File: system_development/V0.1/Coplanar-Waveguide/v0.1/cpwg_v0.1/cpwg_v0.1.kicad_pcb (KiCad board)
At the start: 2 copper layers, 50 x 20 mm, 8 parts, among them J1 142-0761-801, J2 142-0761-801

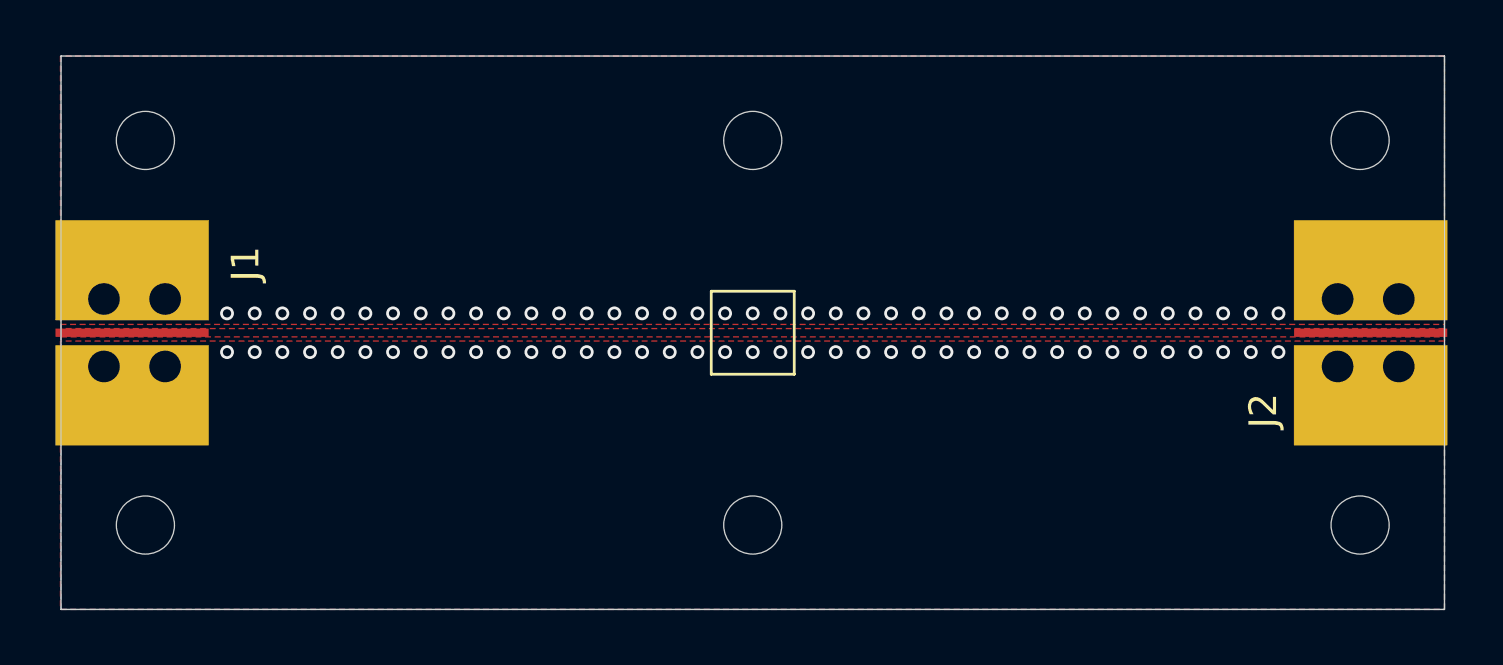
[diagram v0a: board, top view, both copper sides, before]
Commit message: updated silkscreen
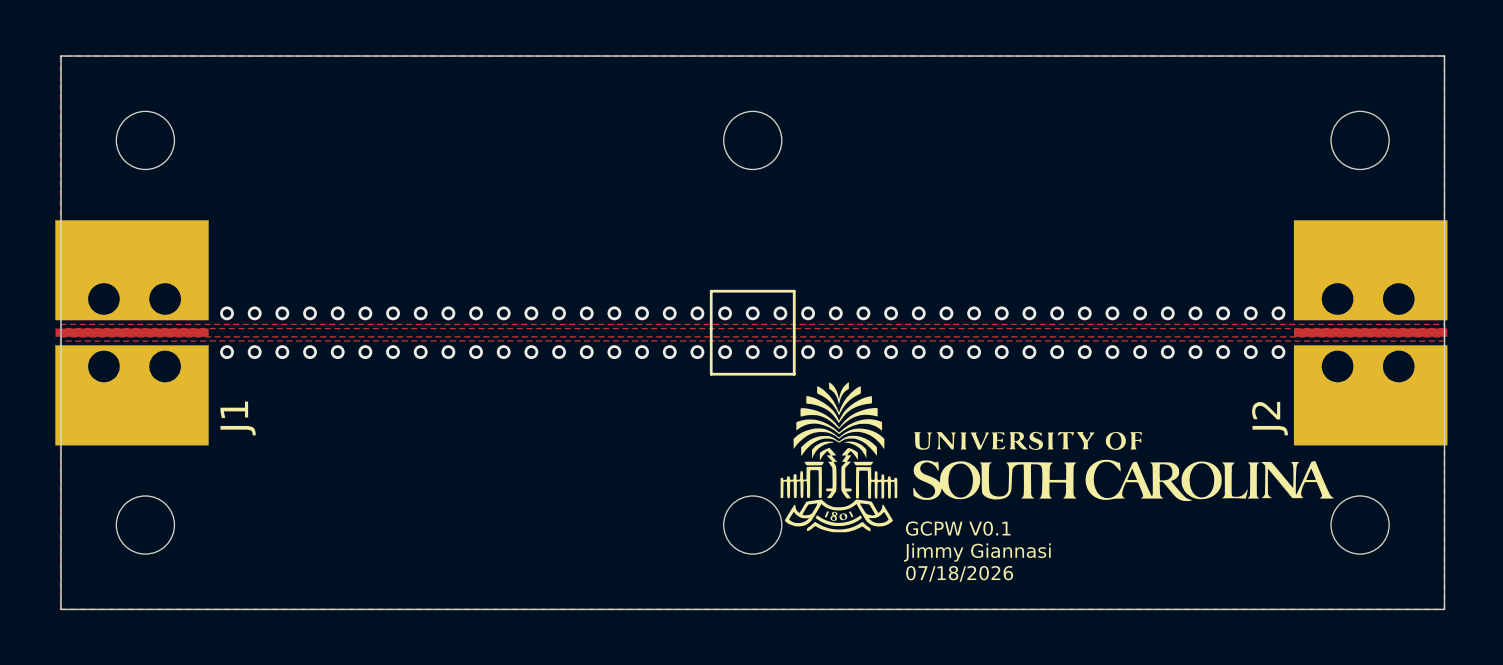
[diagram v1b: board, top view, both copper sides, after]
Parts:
- added G***: LOGO, LOGO, F.Cu at (151.0, 83.0)
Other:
- board text added: "GCPW V0.1 Jimmy Giannasi 07/18/2026"
